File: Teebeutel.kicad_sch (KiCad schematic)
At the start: 163 parts, among them J1 Conn_01x10_Female, J2 Conn_01x10_Female, J3 Micro_SD_Card, J4 RJ45_Shielded, J5 Conn_01x30_Female, J6 Battery, M1 Motor_DC, Q1 S8050, Q2 AO3400, Q3 AO3400, Q4 S8050, Q5 AO3400, Q6 AO3400, Q7 AO3400, SW1 K1-1506SN-01, SW2 SW_SPST, U1 SDB628, U10 TLV70018_SOT23-5, U11 TLV62568DBV, U12 MCP73831-2-OT, U2 RM-V8xxC_TR1, U3 PCA9539BS,118, U4 TXB0104RUT, U5 ESP32-WROOM-32, U6 SRV05-4, U7 SGP30, U8 PPSI262, U9 LIS2DE12

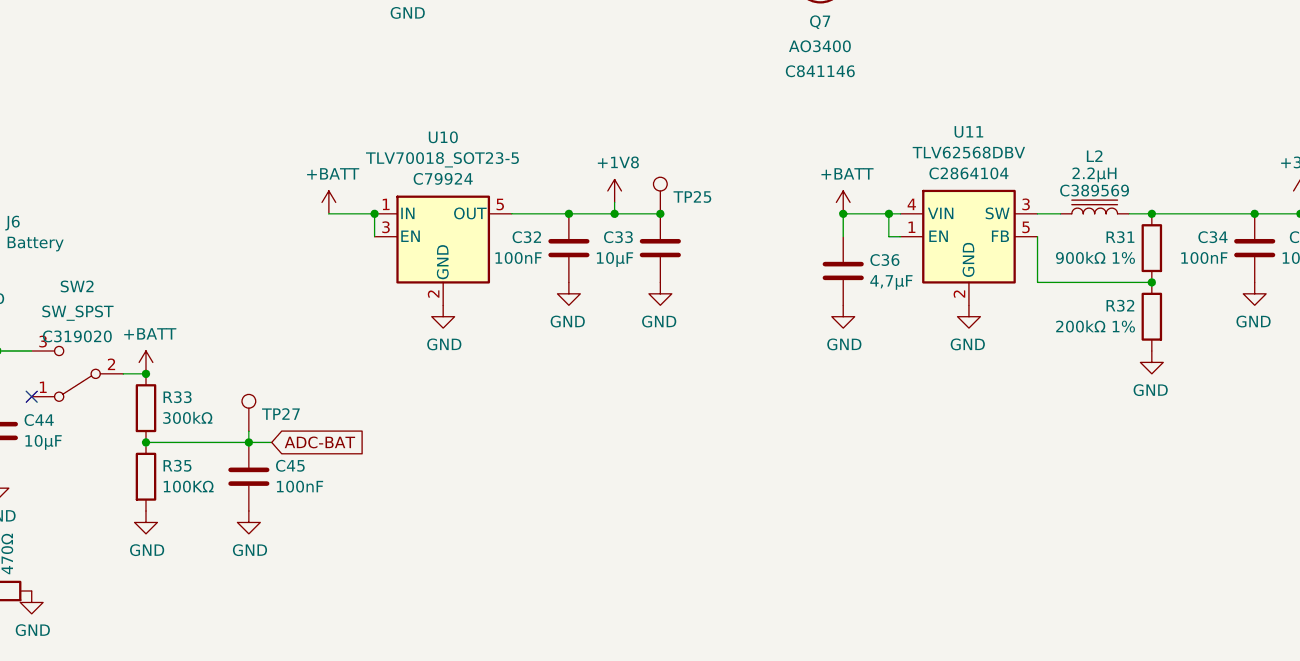
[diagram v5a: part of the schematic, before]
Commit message: feat(sch): Switch DC-DC converter
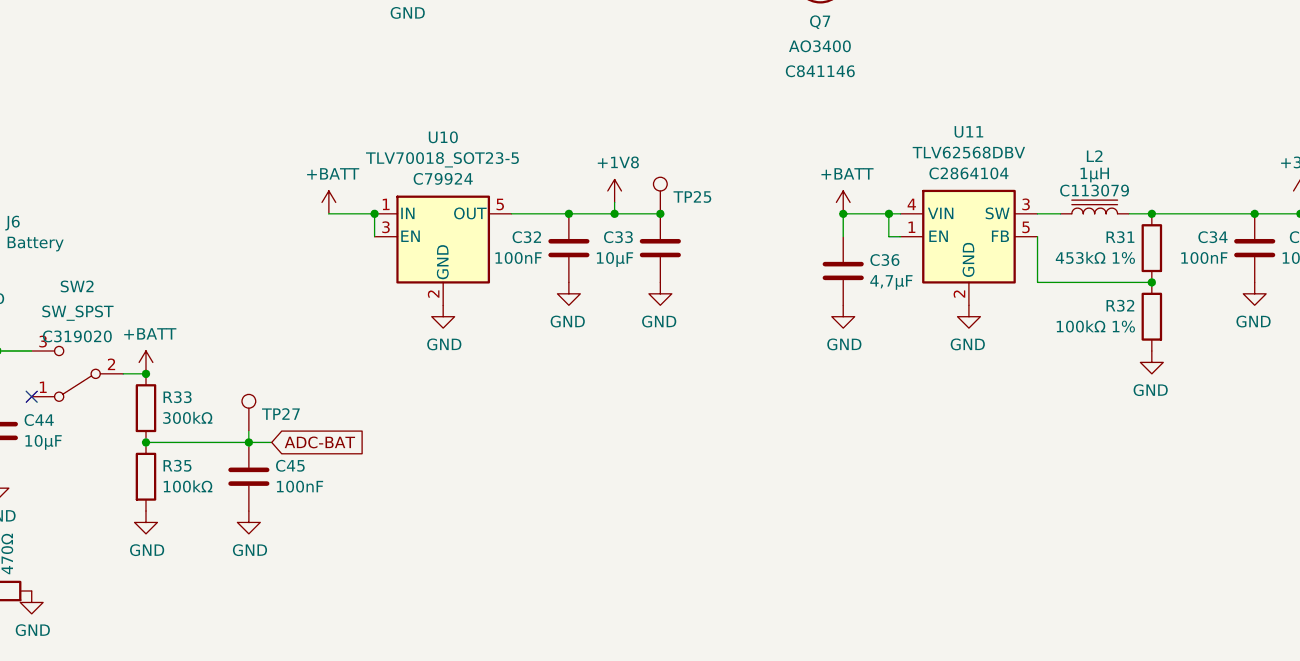
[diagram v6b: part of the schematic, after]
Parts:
- L2: value 2.2µH -> 1µH; LCSC C389569 -> C113079
- R30: LCSC (none) -> C23192
- R31: value 900kΩ 1% -> 453kΩ 1%; LCSC (none) -> C25818
- R32: value 200kΩ 1% -> 100kΩ 1%; LCSC (none) -> C25803
- R35: value 100KΩ -> 100kΩ
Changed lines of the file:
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@@
     (in_bom yes) (on_board yes)
     (property "Reference" "L2" (id 0) (at 372.11 223.52 90))
-    (property "Value" "2.2µH" (id 1) (at 372.11 225.425 90))
+    (property "Value" "1µH" (id 1) (at 372.11 225.425 90))
     (property "Footprint" "Inductor_SMD:L_1210_3225Metric" (id 2) (at 372.11 229.87 0)
       (effects (font (size 1.27 1.27)) hide)
     )
-    (property "Datasheet" "~" (id 3) (at 372.11 229.87 0)
-      (effects (font (size 1.27 1.27)) hide)
-    )
-    (property "LCSC" "C389569" (id 4) (at 372.11 227.33 90))
+    (property "Datasheet" "https://datasheet.lcsc.com/lcsc/1810250908_Murata-Electronics-LQH32PN1R0NN0L_C113079.pdf" (id 3) (at 372.11 229.87 0)
+      (effects (font (size 1.27 1.27)) hide)
+    )
+    (property "LCSC" "C113079" (id 4) (at 372.11 227.33 90))
     (pin "1")
     (pin "2")
@@
       (effects (font (size 1.27 1.27)) (justify left))
     )
-    (property "Value" "200kΩ 1%" (id 1) (at 376.682 242.443 0)
+    (property "Value" "100kΩ 1%" (id 1) (at 376.682 242.443 0)
       (effects (font (size 1.27 1.27)) (justify left))
     )
@@
       (effects (font (size 1.27 1.27)) hide)
     )
+    (property "LCSC" "C25803" (id 5) (at 378.46 241.3 0)
+      (effects (font (size 1.27 1.27)) hide)
+    )
     (pin "1")
     (pin "2")
@@
       (effects (font (size 1.27 1.27)) (justify left))
     )
-    (property "Value" "900kΩ 1%" (id 1) (at 376.682 234.823 0)
+    (property "Value" "453kΩ 1%" (id 1) (at 376.682 234.823 0)
       (effects (font (size 1.27 1.27)) (justify left))
     )
@@
     )
     (property "JLC" "0603" (id 4) (at 378.46 233.68 0)
+      (effects (font (size 1.27 1.27)) hide)
+    )
+    (property "LCSC" "C25818" (id 5) (at 372.745 236.855 0)
       (effects (font (size 1.27 1.27)) hide)
     )
@@
       (effects (font (size 1.27 1.27)) (justify left))
     )
-    (property "Value" "100KΩ" (id 1) (at 268.478 260.223 0)
+    (property "Value" "100kΩ" (id 1) (at 268.478 260.223 0)
       (effects (font (size 1.27 1.27)) (justify left))
     )
@@
       (effects (font (size 1.27 1.27)) hide)
     )
-    (property "LCSC" "" (id 5) (at 233.68 204.47 0)
+    (property "LCSC" "C23192" (id 5) (at 233.68 204.47 0)
       (effects (font (size 1.27 1.27)) hide)
     )
@@
     )
     (path "/00000000-0000-0000-0000-000061e99dac"
-      (reference "L2") (unit 1) (value "2.2µH") (footprint "Inductor_SMD:L_1210_3225Metric")
+      (reference "L2") (unit 1) (value "1µH") (footprint "Inductor_SMD:L_1210_3225Metric")
     )
     (path "/00000000-0000-0000-0000-000062a8ccc2"
@@
     )
     (path "/00000000-0000-0000-0000-000061f21ba3"
-      (reference "R31") (unit 1) (value "900kΩ 1%") (footprint "Resistor_SMD:R_0603_1608Metric")
+      (reference "R31") (unit 1) (value "453kΩ 1%") (footprint "Resistor_SMD:R_0603_1608Metric")
     )
     (path "/00000000-0000-0000-0000-000061f21b9b"
-      (reference "R32") (unit 1) (value "200kΩ 1%") (footprint "Resistor_SMD:R_0603_1608Metric")
+      (reference "R32") (unit 1) (value "100kΩ 1%") (footprint "Resistor_SMD:R_0603_1608Metric")
     )
     (path "/00000000-0000-0000-0000-00006224d4e7"
@@
     )
     (path "/00000000-0000-0000-0000-00006224e631"
-      (reference "R35") (unit 1) (value "100KΩ") (footprint "Resistor_SMD:R_0603_1608Metric")
+      (reference "R35") (unit 1) (value "100kΩ") (footprint "Resistor_SMD:R_0603_1608Metric")
     )
     (path "/00000000-0000-0000-0000-00006195b033"

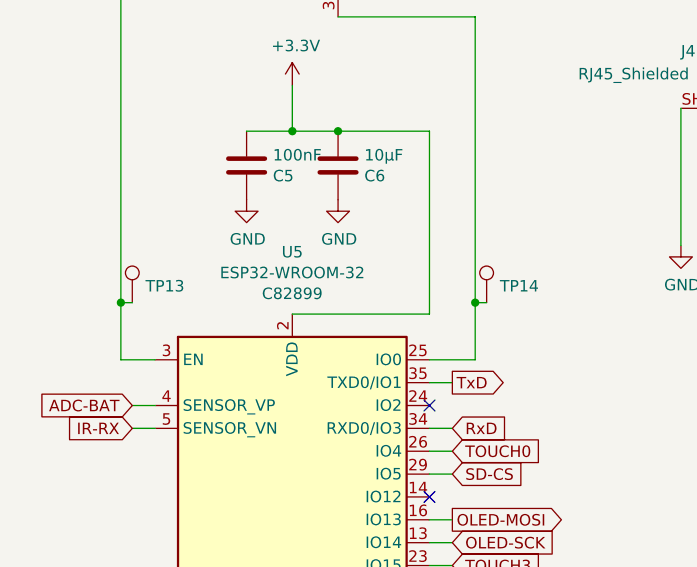
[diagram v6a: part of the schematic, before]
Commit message: feat(esp): Upgrade to latest ESP32-WROOM with 16MB flash
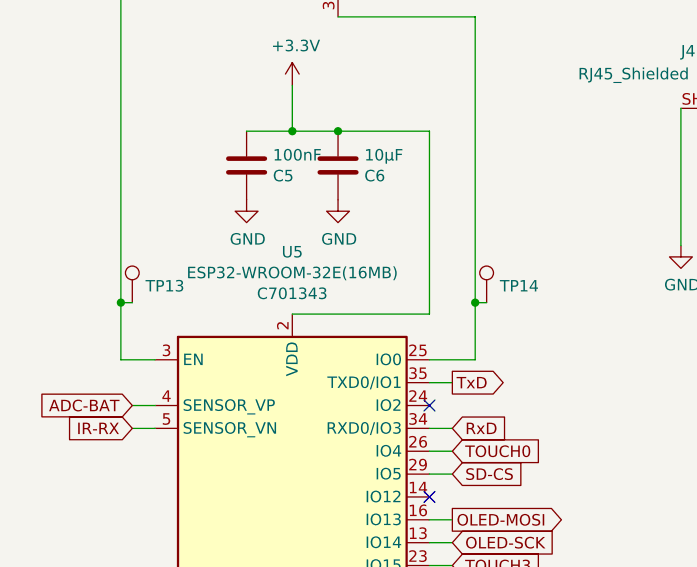
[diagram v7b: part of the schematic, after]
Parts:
- U5: value ESP32-WROOM-32 -> ESP32-WROOM-32E(16MB); JLC QFN-38_EP_18.0x25.0x1.27P -> (none); LCSC C82899 -> C701343
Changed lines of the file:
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@@
     (in_bom yes) (on_board yes)
     (property "Reference" "U5" (id 0) (at 46.99 70.5866 0))
-    (property "Value" "ESP32-WROOM-32" (id 1) (at 46.99 72.898 0))
+    (property "Value" "ESP32-WROOM-32E(16MB)" (id 1) (at 46.99 72.898 0))
     (property "Footprint" "RF_Module:ESP32-WROOM-32" (id 2) (at 46.99 151.13 0)
       (effects (font (size 1.27 1.27)) hide)
     )
-    (property "Datasheet" "https://www.espressif.com/sites/default/files/documentation/esp32-wroom-32_datasheet_en.pdf" (id 3) (at 39.37 111.76 0)
-      (effects (font (size 1.27 1.27)) hide)
-    )
-    (property "LCSC" "C82899" (id 4) (at 46.99 75.2094 0))
-    (property "JLC" "QFN-38_EP_18.0x25.0x1.27P" (id 5) (at 46.99 113.03 0)
+    (property "Datasheet" "https://www.espressif.com/sites/default/files/documentation/esp32-wroom-32e_esp32-wroom-32ue_datasheet_en.pdf" (id 3) (at 39.37 111.76 0)
       (effects (font (size 1.27 1.27)) hide)
     )
+    (property "LCSC" "C701343" (id 4) (at 46.99 75.2094 0))
     (pin "1")
     (pin "10")
@@
     )
     (path "/00000000-0000-0000-0000-000061827961"
-      (reference "U5") (unit 1) (value "ESP32-WROOM-32") (footprint "RF_Module:ESP32-WROOM-32")
+      (reference "U5") (unit 1) (value "ESP32-WROOM-32E(16MB)") (footprint "RF_Module:ESP32-WROOM-32")
     )
     (path "/00000000-0000-0000-0000-000061c99717"

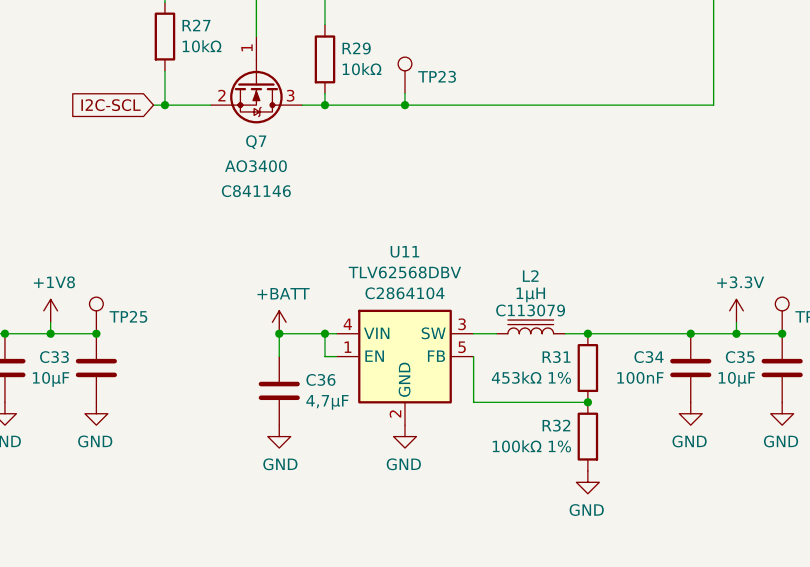
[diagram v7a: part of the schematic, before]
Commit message: feat(sch): Switch DC-DC converter
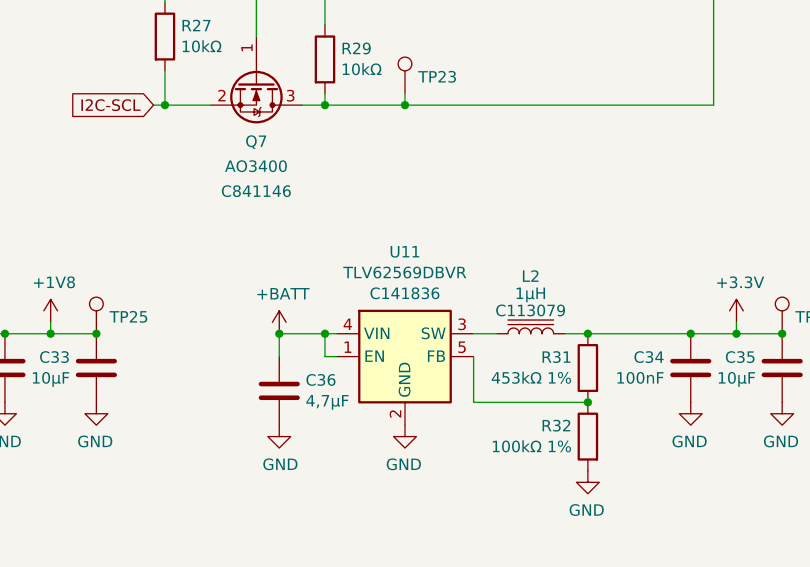
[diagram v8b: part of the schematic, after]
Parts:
- U11: value TLV62568DBV -> TLV62569DBVR; LCSC C2864104 -> C141836
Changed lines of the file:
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@@
     (in_bom yes) (on_board yes)
     (property "Reference" "U11" (id 0) (at 358.14 220.8022 0))
-    (property "Value" "TLV62568DBV" (id 1) (at 358.14 223.1136 0))
+    (property "Value" "TLV62569DBVR" (id 1) (at 358.14 223.1136 0))
     (property "Footprint" "Package_TO_SOT_SMD:SOT-23-5" (id 2) (at 359.41 238.76 0)
       (effects (font (size 1.27 1.27) italic) (justify left) hide)
     )
-    (property "Datasheet" "http://www.ti.com/lit/ds/symlink/tlv62568.pdf" (id 3) (at 351.79 220.98 0)
-      (effects (font (size 1.27 1.27)) hide)
-    )
-    (property "LCSC" "C2864104" (id 4) (at 358.14 225.425 0))
+    (property "Datasheet" "https://www.ti.com/lit/ds/symlink/tlv62569.pdf" (id 3) (at 351.79 220.98 0)
+      (effects (font (size 1.27 1.27)) hide)
+    )
+    (property "LCSC" "C141836" (id 4) (at 358.14 225.425 0))
     (pin "1")
     (pin "2")
@@
     )
     (path "/00000000-0000-0000-0000-000061cbde0a"
-      (reference "U11") (unit 1) (value "TLV62568DBV") (footprint "Package_TO_SOT_SMD:SOT-23-5")
+      (reference "U11") (unit 1) (value "TLV62569DBVR") (footprint "Package_TO_SOT_SMD:SOT-23-5")
     )
     (path "/00000000-0000-0000-0000-0000618b7477"
